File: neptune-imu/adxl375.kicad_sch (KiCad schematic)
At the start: 4 parts, among them U3 ADXL375BCCZ

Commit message: Pécsi folytatja a cuccost
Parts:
- U3: footprint szar:LGA-14_L5.0-W3.0-P0.80-BL-1 -> (none)
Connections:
- net +3.3V: no longer C10.2, U3.1 (VDDI/O)
- net SPI1_MISO renamed MISO_1v8
- net SPI1_MOSI renamed MOSI_1v8
- net SPI1_SCK renamed SCK_1v8
- new net +1V8: C10.2, U3.1 (VDDI/O)
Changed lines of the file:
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@@
 		)
 	)
-	(text_box "Precision Temperature Sensor (RTD) nr 1.\n"
+	(text_box "Accelerometer nr 1.\n"
 		(exclude_from_sim no)
 		(at 19.05 17.78 0)
@@
 		)
 	)
-	(global_label "SPI1_MISO"
-		(shape output)
-		(at 102.87 46.99 0)
+	(global_label "SCK_1v8"
+		(shape input)
+		(at 102.87 41.91 0)
 		(fields_autoplaced yes)
 		(effects
@@
 		)
 		(property "Intersheetrefs" "${INTERSHEET_REFS}"
-			(at 115.7128 46.99 0)
+			(at 113.9589 41.91 0)
 			(effects
 				(font
@@
 		)
 	)
-	(global_label "SPI1_SCK"
+	(global_label "MOSI_1v8"
 		(shape input)
-		(at 102.87 41.91 0)
+		(at 102.87 44.45 0)
 		(fields_autoplaced yes)
 		(effects
@@
 		)
 		(property "Intersheetrefs" "${INTERSHEET_REFS}"
-			(at 114.8661 41.91 0)
+			(at 114.8056 44.45 0)
 			(effects
 				(font
@@
 		)
 	)
-	(global_label "SPI1_MOSI"
-		(shape input)
-		(at 102.87 44.45 0)
+	(global_label "MISO_1v8"
+		(shape output)
+		(at 102.87 46.99 0)
 		(fields_autoplaced yes)
 		(effects
@@
 		)
 		(property "Intersheetrefs" "${INTERSHEET_REFS}"
-			(at 115.7128 44.45 0)
+			(at 114.8056 46.99 0)
 			(effects
 				(font
@@
 	)
 	(symbol
-		(lib_id "power:+3.3V")
-		(at 50.8 41.91 90)
-		(unit 1)
-		(exclude_from_sim no)
-		(in_bom yes)
-		(on_board yes)
-		(dnp no)
-		(fields_autoplaced yes)
-		(property "Reference" "#PWR018"
-			(at 54.61 41.91 0)
-			(effects
-				(font
-					(size 1.27 1.27)
-				)
-				(hide yes)
-			)
-		)
-		(property "Value" "+3.3V"
-			(at 46.99 41.9099 90)
-			(effects
-				(font
-					(size 1.27 1.27)
-				)
-				(justify left)
-			)
-		)
-		(property "Footprint" ""
-			(at 50.8 41.91 0)
-			(effects
-				(font
-					(size 1.27 1.27)
-				)
-				(hide yes)
-			)
-		)
-		(property "Datasheet" ""
-			(at 50.8 41.91 0)
-			(effects
-				(font
-					(size 1.27 1.27)
-				)
-				(hide yes)
-			)
-		)
-		(property "Description" "Power symbol creates a global label with name \"+3.3V\""
-			(at 50.8 41.91 0)
-			(effects
-				(font
-					(size 1.27 1.27)
-				)
-				(hide yes)
-			)
-		)
-		(pin "1"
-		)
-		(instances
-			(project "neptune-imu"
-				(path "/5267d5be-f3eb-4ed0-80b1-f192444f0b69/c385354e-c644-4b4a-bcac-6e87af3cb5e2"
-					(reference "#PWR018")
-					(unit 1)
-				)
-			)
-		)
-	)
-	(symbol
 		(lib_id "power:GND")
 		(at 53.34 52.07 270)
@@
 	)
 	(symbol
+		(lib_id "power:+1V8")
+		(at 50.8 41.91 90)
+		(unit 1)
+		(exclude_from_sim no)
+		(in_bom yes)
+		(on_board yes)
+		(dnp no)
+		(fields_autoplaced yes)
+		(property "Reference" "#PWR018"
+			(at 54.61 41.91 0)
+			(effects
+				(font
+					(size 1.27 1.27)
+				)
+				(hide yes)
+			)
+		)
+		(property "Value" "+1V8"
+			(at 46.99 41.9099 90)
+			(effects
+				(font
+					(size 1.27 1.27)
+				)
+				(justify left)
+			)
+		)
+		(property "Footprint" ""
+			(at 50.8 41.91 0)
+			(effects
+				(font
+					(size 1.27 1.27)
+				)
+				(hide yes)
+			)
+		)
+		(property "Datasheet" ""
+			(at 50.8 41.91 0)
+			(effects
+				(font
+					(size 1.27 1.27)
+				)
+				(hide yes)
+			)
+		)
+		(property "Description" "Power symbol creates a global label with name \"+1V8\""
+			(at 50.8 41.91 0)
+			(effects
+				(font
+					(size 1.27 1.27)
+				)
+				(hide yes)
+			)
+		)
+		(pin "1"
+		)
+		(instances
+			(project ""
+				(path "/5267d5be-f3eb-4ed0-80b1-f192444f0b69/c385354e-c644-4b4a-bcac-6e87af3cb5e2"
+					(reference "#PWR018")
+					(unit 1)
+				)
+			)
+		)
+	)
+	(symbol
 		(lib_id "Device:C_Small")
 		(at 53.34 35.56 0)
@@
 			)
 		)
-		(property "Footprint" "szar:LGA-14_L5.0-W3.0-P0.80-BL-1"
+		(property "Footprint" ""
 			(at 78.74 64.77 0)
 			(effects

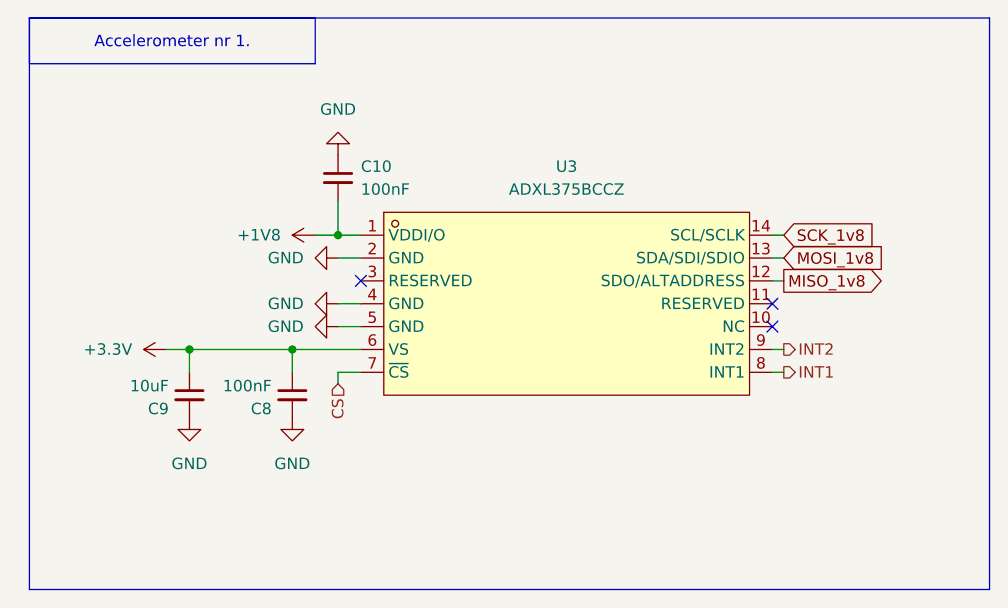
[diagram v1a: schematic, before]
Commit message: level shifter(bss138) + icm20948 + int lines needed
Also some final things like star(orientattion)
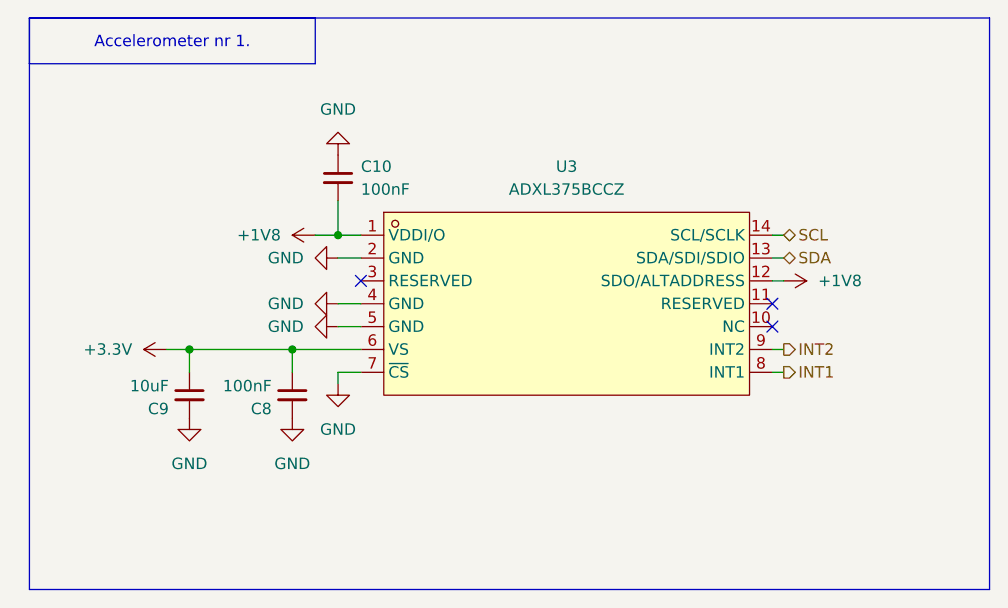
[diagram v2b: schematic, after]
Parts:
- C10, C8: footprint (none) -> Capacitor_SMD:C_0402_1005Metric
- C9: footprint (none) -> Capacitor_SMD:C_0603_1608Metric
- U3: footprint (none) -> neptune-imu-footprints:LGA-14_L5.0-W3.0-P0.80-BL-1
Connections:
- net CS is gone; now on net GND: U3.7 (~{CS})
- net MISO_1v8 is gone; now on net +1V8: U3.12 (SDO/ALTADDRESS)
- net MOSI_1v8 renamed SDA
- net SCK_1v8 renamed SCL
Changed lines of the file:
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@@
 		)
 	)
-	(global_label "SCK_1v8"
-		(shape input)
-		(at 102.87 41.91 0)
-		(fields_autoplaced yes)
+	(hierarchical_label "SDA"
+		(shape bidirectional)
+		(at 102.87 44.45 0)
 		(effects
 			(font
@@
 			(justify left)
 		)
-		(property "Intersheetrefs" "${INTERSHEET_REFS}"
-			(at 113.9589 41.91 0)
-			(effects
-				(font
-					(size 1.27 1.27)
-				)
-				(justify left)
-				(hide yes)
-			)
-		)
-	)
-	(global_label "MOSI_1v8"
-		(shape input)
-		(at 102.87 44.45 0)
-		(fields_autoplaced yes)
+	)
+	(hierarchical_label "SCL"
+		(shape bidirectional)
+		(at 102.87 41.91 0)
 		(effects
 			(font
@@
 			)
 			(justify left)
-		)
-		(property "Intersheetrefs" "${INTERSHEET_REFS}"
-			(at 114.8056 44.45 0)
-			(effects
-				(font
-					(size 1.27 1.27)
-				)
-				(justify left)
-				(hide yes)
-			)
-		)
-	)
-	(global_label "MISO_1v8"
-		(shape output)
-		(at 102.87 46.99 0)
-		(fields_autoplaced yes)
-		(effects
-			(font
-				(size 1.27 1.27)
-			)
-			(justify left)
-		)
-		(property "Intersheetrefs" "${INTERSHEET_REFS}"
-			(at 114.8056 46.99 0)
-			(effects
-				(font
-					(size 1.27 1.27)
-				)
-				(justify left)
-				(hide yes)
-			)
-		)
-	)
-	(hierarchical_label "CS"
-		(shape input)
-		(at 53.34 58.42 270)
-		(effects
-			(font
-				(size 1.27 1.27)
-			)
-			(justify right)
 		)
 	)
@@
 	(symbol
 		(lib_id "power:GND")
+		(at 53.34 58.42 0)
+		(unit 1)
+		(exclude_from_sim no)
+		(in_bom yes)
+		(on_board yes)
+		(dnp no)
+		(fields_autoplaced yes)
+		(property "Reference" "#PWR028"
+			(at 53.34 64.77 0)
+			(effects
+				(font
+					(size 1.27 1.27)
+				)
+				(hide yes)
+			)
+		)
+		(property "Value" "GND"
+			(at 53.34 63.5 0)
+			(effects
+				(font
+					(size 1.27 1.27)
+				)
+			)
+		)
+		(property "Footprint" ""
+			(at 53.34 58.42 0)
+			(effects
+				(font
+					(size 1.27 1.27)
+				)
+				(hide yes)
+			)
+		)
+		(property "Datasheet" ""
+			(at 53.34 58.42 0)
+			(effects
+				(font
+					(size 1.27 1.27)
+				)
+				(hide yes)
+			)
+		)
+		(property "Description" "Power symbol creates a global label with name \"GND\" , ground"
+			(at 53.34 58.42 0)
+			(effects
+				(font
+					(size 1.27 1.27)
+				)
+				(hide yes)
+			)
+		)
+		(pin "1"
+		)
+		(instances
+			(project "neptune-imu"
+				(path "/5267d5be-f3eb-4ed0-80b1-f192444f0b69/c385354e-c644-4b4a-bcac-6e87af3cb5e2"
+					(reference "#PWR028")
+					(unit 1)
+				)
+			)
+		)
+	)
+	(symbol
+		(lib_id "power:GND")
 		(at 48.26 62.23 0)
 		(unit 1)
@@
 			)
 		)
-		(property "Footprint" ""
+		(property "Footprint" "Capacitor_SMD:C_0402_1005Metric"
 			(at 48.26 59.69 0)
 			(effects
@@
 			)
 		)
-		(property "Footprint" ""
+		(property "Footprint" "Capacitor_SMD:C_0603_1608Metric"
 			(at 36.83 59.69 0)
 			(effects
@@
 	(symbol
 		(lib_id "power:+1V8")
+		(at 102.87 46.99 270)
+		(unit 1)
+		(exclude_from_sim no)
+		(in_bom yes)
+		(on_board yes)
+		(dnp no)
+		(fields_autoplaced yes)
+		(property "Reference" "#PWR034"
+			(at 99.06 46.99 0)
+			(effects
+				(font
+					(size 1.27 1.27)
+				)
+				(hide yes)
+			)
+		)
+		(property "Value" "+1V8"
+			(at 106.68 46.9899 90)
+			(effects
+				(font
+					(size 1.27 1.27)
+				)
+				(justify left)
+			)
+		)
+		(property "Footprint" ""
+			(at 102.87 46.99 0)
+			(effects
+				(font
+					(size 1.27 1.27)
+				)
+				(hide yes)
+			)
+		)
+		(property "Datasheet" ""
+			(at 102.87 46.99 0)
+			(effects
+				(font
+					(size 1.27 1.27)
+				)
+				(hide yes)
+			)
+		)
+		(property "Description" "Power symbol creates a global label with name \"+1V8\""
+			(at 102.87 46.99 0)
+			(effects
+				(font
+					(size 1.27 1.27)
+				)
+				(hide yes)
+			)
+		)
+		(pin "1"
+		)
+		(instances
+			(project "neptune-imu"
+				(path "/5267d5be-f3eb-4ed0-80b1-f192444f0b69/c385354e-c644-4b4a-bcac-6e87af3cb5e2"
+					(reference "#PWR034")
+					(unit 1)
+				)
+			)
+		)
+	)
+	(symbol
+		(lib_id "power:+1V8")
 		(at 50.8 41.91 90)
 		(unit 1)
@@
 			)
 		)
-		(property "Footprint" ""
+		(property "Footprint" "Capacitor_SMD:C_0402_1005Metric"
 			(at 53.34 35.56 0)
 			(effects
@@
 			)
 		)
-		(property "Footprint" ""
+		(property "Footprint" "neptune-imu-footprints:LGA-14_L5.0-W3.0-P0.80-BL-1"
 			(at 78.74 64.77 0)
 			(effects

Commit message: fixing bugs, production
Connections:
- net +3.3V: now also C10.2, U3.1 (VDDI/O), U3.7 (~{CS})
- net GND: now also U3.12 (SDO/ALTADDRESS); no longer U3.7 (~{CS})
- removed net +1V8: C10.2, U3.1 (VDDI/O), U3.12 (SDO/ALTADDRESS)
